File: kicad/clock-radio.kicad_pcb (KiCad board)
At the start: 4 copper layers, 214 x 122 mm, 49 parts, among them J1 Rotary Encoder Header, J2 Antenna, J3 USB_C_Receptacle_USB2.0_16P, J4 SWD Header, J5 Display Header, J6 Speaker Header, SW1 BOOT0, U1 DS3231MZ, U2 STM32G0B1CETx, U3 RDA5807M_Module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

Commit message: updated pcb layout
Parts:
- R13, R8, R9: footprint Resistor_SMD:R_0201_0603Metric_Pad0.64x0.40mm_HandSolder -> Resistor_SMD:R_0402_1005Metric_Pad0.72x0.64mm_HandSolder
- moved C20 73.1 mm to (161.1, 39.4), turned to 180 degrees
- moved R13 56.3 mm to (161.1, 38.0), turned to 180 degrees
- moved R1 51.8 mm to (148.4, 58.6), turned to 180 degrees
- moved R4 50.1 mm to (164.2, 57.0), turned to 90 degrees
- moved C17 49.4 mm to (161.2, 43.0)
- moved C4 49.4 mm to (167.0, 48.6), turned to 90 degrees
- moved C18 49.1 mm to (161.2, 41.4)
- moved R8 48.4 mm to (156.5, 46.6), turned to 90 degrees
- moved R6 48.3 mm to (162.6, 57.0), turned to 90 degrees
- moved R9 45.9 mm to (151.8, 46.6), turned to 90 degrees
- moved J2 45.8 mm to (133.2, 46.4)
- moved C3 39.8 mm to (156.8, 63.2)
- moved J1 39.3 mm to (125.6, 53.9)
- moved C1 38.3 mm to (155.4, 62.0), turned to 180 degrees
- moved C2 37.9 mm to (155.4, 60.8), turned to 180 degrees
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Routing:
- net GND: track 0.00 -> 30.5 mm, vias 0 -> 7
- net SDA: track 0.00 -> 25.0 mm, vias 0 -> 1
- net SCL: track 0.00 -> 25.0 mm, vias 0 -> 2
- net +3V3: track 0.00 -> 18.2 mm, vias 0 -> 2
- net RTC_INT: track 0.00 -> 16.9 mm, vias 0 -> 2
- net +5V: track 0.00 -> 15.3 mm, vias 0 -> 5
- net SWCLK: track 0.00 -> 6.53 mm
- net Net-(J3-SHIELD): track 0.00 -> 5.99 mm
- net Net-(U2-PF2): track 0.00 -> 4.82 mm
- net Net-(J3-CC1): track 0.00 -> 3.52 mm
- net Net-(J3-CC2): track 0.00 -> 3.13 mm
- net Net-(R1-Pad2): track 0.00 -> 2.40 mm
- net Net-(J3-D--PadA7): track 6.08 -> 4.77 mm
- added copper zone on F.Cu, net +5V
- added copper zone on F.Cu, net GND
- added copper zone on F.Cu, net Net-(U2-VBAT)
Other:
- board size 214 x 122 mm -> 35 x 35 mm

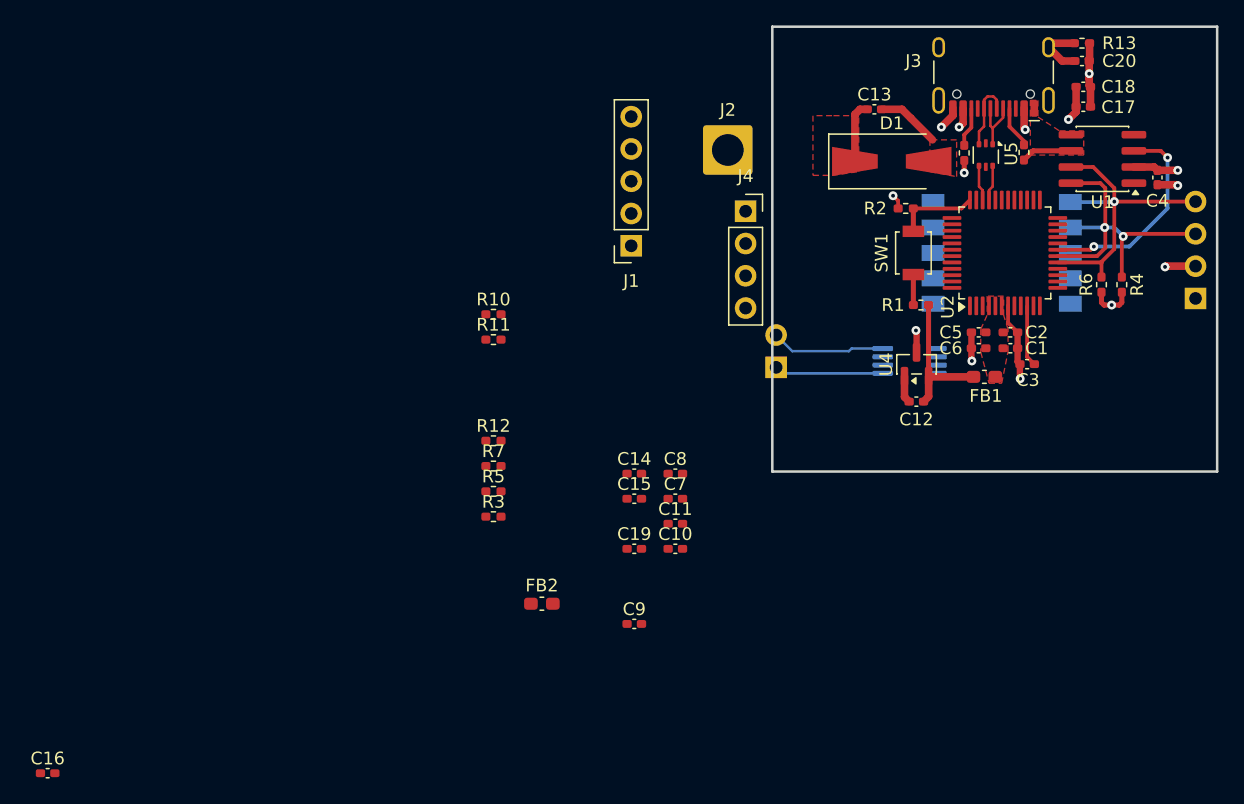
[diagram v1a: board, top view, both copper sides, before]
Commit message: connected all components and added in ground and power plane
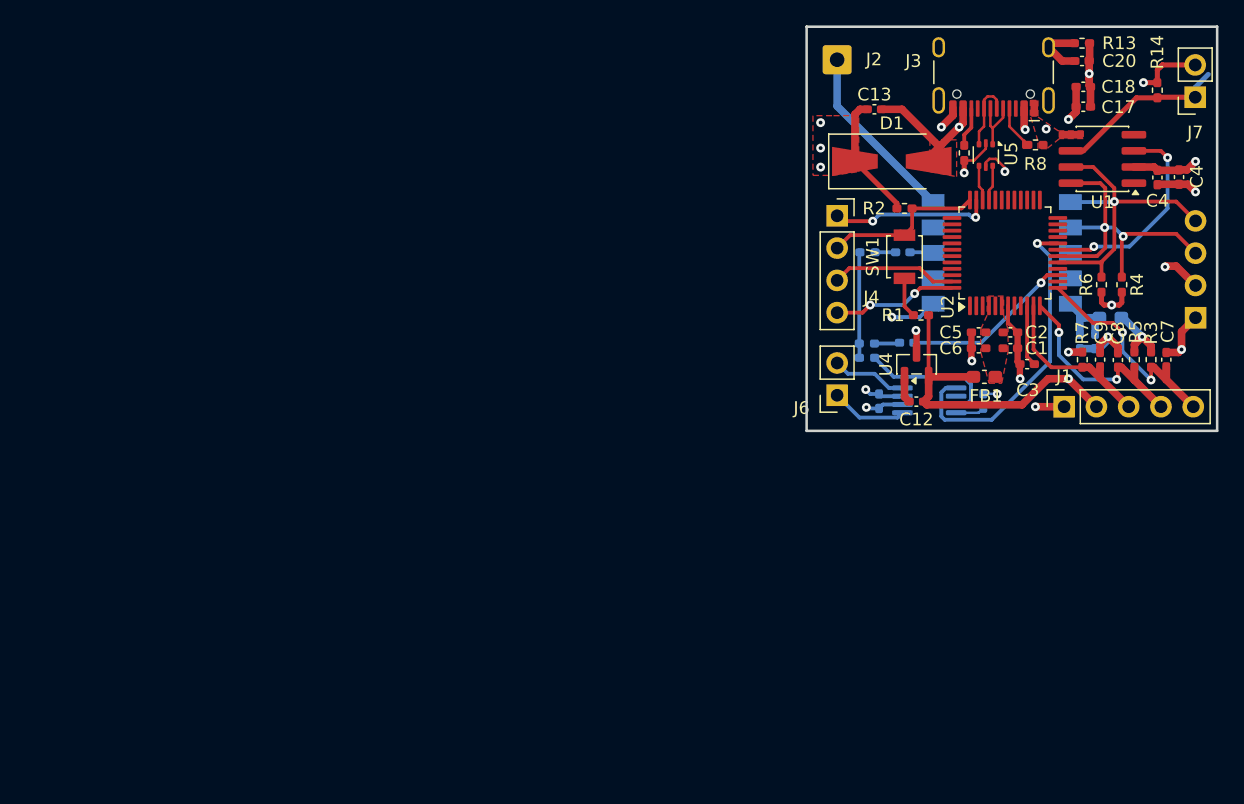
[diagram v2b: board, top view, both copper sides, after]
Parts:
- added C4: 100n, Capacitor_SMD:C_0402_1005Metric_Pad0.74x0.62mm_HandSolder, F.Cu at (168.7, 48.5)
- added J7: Coin Cell, Connector_PinSocket_2.54mm:PinSocket_1x02_P2.54mm_Vertical, F.Cu at (170.0, 42.2)
- added R14: 0, Resistor_SMD:R_0402_1005Metric_Pad0.72x0.64mm_HandSolder, F.Cu at (167.0, 41.7)
- C10, C11, C14, C15, C16, C19, FB2, R10, R11, R12: moved to B.Cu
- J2: footprint Connector_Wire:SolderWire-2sqmm_1x01_D2mm_OD3.9mm -> Connector_Wire:SolderWire-0.5sqmm_1x01_D0.9mm_OD2.3mm
- J6: moved to F.Cu
- moved C16 79.2 mm to (153.3, 66.2), turned to 90 degrees
- moved R3 53.2 mm to (166.5, 62.9), turned to 90 degrees
- moved R5 51.5 mm to (165.2, 62.9), turned to 90 degrees
- moved FB2 50.1 mm to (163.3, 59.6), turned to 180 degrees
- moved R7 47.1 mm to (161.1, 62.9), turned to 90 degrees
- moved C9 42.1 mm to (162.5, 62.9), turned to 90 degrees
- moved C7 40.1 mm to (167.7, 62.9), turned to 90 degrees
- moved C10 36.8 mm to (162.1, 61.5), turned to -90 degrees
- moved J1 36.3 mm to (159.7, 66.6), turned to 90 degrees
- moved C8 35.9 mm to (163.9, 62.9), turned to 90 degrees
- moved C11 34.9 mm to (160.9, 61.5), turned to -90 degrees
- moved R12 30.1 mm to (144.2, 62.8)
- moved R10 29.8 mm to (144.2, 54.5), turned to 180 degrees
- moved R11 29.4 mm to (144.1, 61.6)
- moved C14 27.4 mm to (147.0, 54.5), turned to 180 degrees
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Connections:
- U1 pad 6: GND -> Net-(J7-Pin_1)
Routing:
- net +5V: track 15.3 -> 62.5 mm, vias 5 -> 7
- net +3V3: track 18.2 -> 56.8 mm, vias 2 -> 5
- net GND: track 30.5 -> 61.5 mm, vias 7 -> 17
- net SD: track 0.00 -> 25.1 mm, vias 0 -> 1
- net Button: track 0.00 -> 17.8 mm, vias 0 -> 2
- net TIM2_CH2: track 0.00 -> 16.5 mm, vias 0 -> 2
- net Net-(J2-Pin_1): track 0.00 -> 14.3 mm
- net Net-(J7-Pin_1): track 0.00 -> 13.7 mm
- net TIM2_CH1: track 0.00 -> 13.7 mm
- net DAC1: track 0.00 -> 13.6 mm, vias 0 -> 1
- net SWDIO: track 0.00 -> 12.8 mm, vias 0 -> 2
- net Net-(U6-IN+): track 0.00 -> 11.0 mm
- net UART_TX: track 0.00 -> 9.87 mm
- net UART_RX: track 0.00 -> 9.85 mm, vias 0 -> 2
- net Net-(R10-Pad2): track 0.00 -> 8.26 mm
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- added copper zone on In2.Cu, net +3V3
- added copper zone on In2.Cu, net +5V
- added copper zone on In1.Cu, net GND
- added copper zone on In1.Cu, net Net-(J3-SHIELD)
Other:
- board size 35 x 35 mm -> 32.3 x 31.8 mm

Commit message: Check out antenna footprint
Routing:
- net GND: track 61.5 -> 65.3 mm
- net Net-(J7-Pin_1): track 13.7 -> 11.5 mm
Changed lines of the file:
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@@
 		(tags "Through hole socket strip THT 1x02 2.54mm single row")
 		(property "Reference" "J6"
-			(at 2.8 -1 0)
+			(at -3.2 -0.05 0)
 			(layer "F.SilkS")
 			(effects
@@
 		(tags "MSOP SO")
 		(property "Reference" "U6"
-			(at 0 2.45 0)
+			(at 0 2.2 0)
 			(layer "B.SilkS")
 			(effects
@@
 		(tags "resistor handsolder")
 		(property "Reference" "R12"
-			(at -2.7025 0 0)
+			(at -0.1525 1.25 0)
 			(layer "B.SilkS")
 			(effects
@@
 		(tags "resistor handsolder")
 		(property "Reference" "R11"
-			(at -2.690541 -0.028809 0)
+			(at -0.140541 -1.128809 0)
 			(layer "B.SilkS")
 			(effects
@@
 	)
 	(segment
+		(start 146.515 65.25)
+		(end 144.05 65.25)
+		(width 0.6)
+		(layer "F.Cu")
+		(net 1)
+	)
+	(segment
 		(start 169.4 49.1)
 		(end 170 49.7)
@@
 	)
 	(segment
+		(start 147.465 66.2)
+		(end 146.515 65.25)
+		(width 0.6)
+		(layer "F.Cu")
+		(net 1)
+	)
+	(segment
 		(start 153.5 45.875)
 		(end 153.5 46.3)
@@
 		(net 74)
 	)
-	(segment
-		(start 169.975 42.25)
-		(end 169.975 41.477767)
-		(width 0.4)
-		(layer "B.Cu")
-		(net 74)
-	)
-	(segment
-		(start 169.975 41.477767)
-		(end 171 40.452767)
-		(width 0.4)
-		(layer "B.Cu")
-		(net 74)
-	)

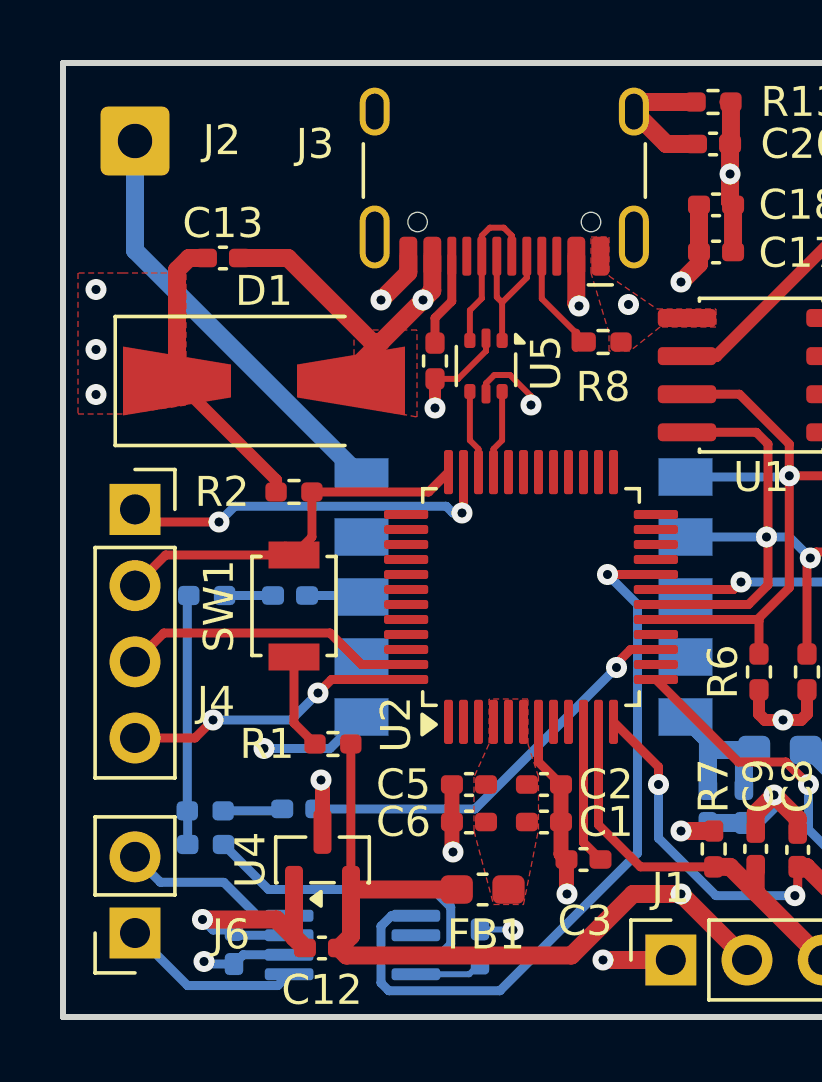
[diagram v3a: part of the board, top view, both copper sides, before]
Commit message: swapped layers
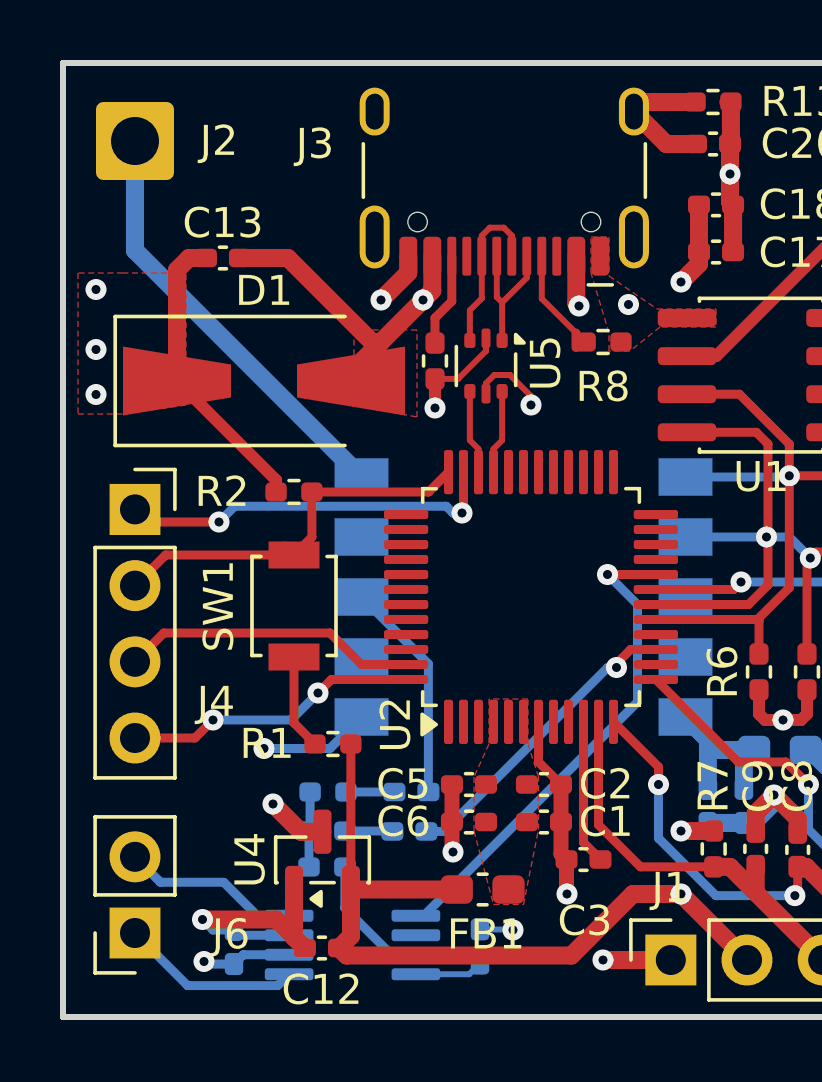
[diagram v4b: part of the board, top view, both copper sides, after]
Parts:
- J2: footprint Connector_Wire:SolderWire-0.5sqmm_1x01_D0.9mm_OD2.3mm -> Connector_Wire:SolderWire-0.75sqmm_1x01_D1.25mm_OD2.3mm
- moved R10 7.70 mm to (148.2, 61.0)
- moved C14 7.70 mm to (151.0, 61.0)
- moved R12 4.11 mm to (148.2, 63.5)
- moved R11 4.11 mm to (148.2, 62.3)
- moved C15 3.75 mm to (150.9, 62.3)
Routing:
- net +5V: track 62.5 -> 26.3 mm
- net +3V3: track 56.8 -> 41.0 mm
- net SD: track 25.1 -> 16.6 mm
- net Net-(U6-IN+): track 11.0 -> 4.38 mm
- net Net-(R10-Pad2): track 8.26 -> 2.52 mm
- net Net-(U3-LOUT): track 1.84 -> 7.49 mm
- net DAC1: track 13.6 -> 10.2 mm
- added copper zone on In1.Cu, net +3V3
- added copper zone on In1.Cu, net +5V
- added copper zone on In2.Cu, net GND
- added copper zone on In2.Cu, net Net-(J3-SHIELD)
- removed copper zone on In2.Cu, net +3V3
- removed copper zone on In2.Cu, net +5V
- removed copper zone on In1.Cu, net GND
- removed copper zone on In1.Cu, net Net-(J3-SHIELD)

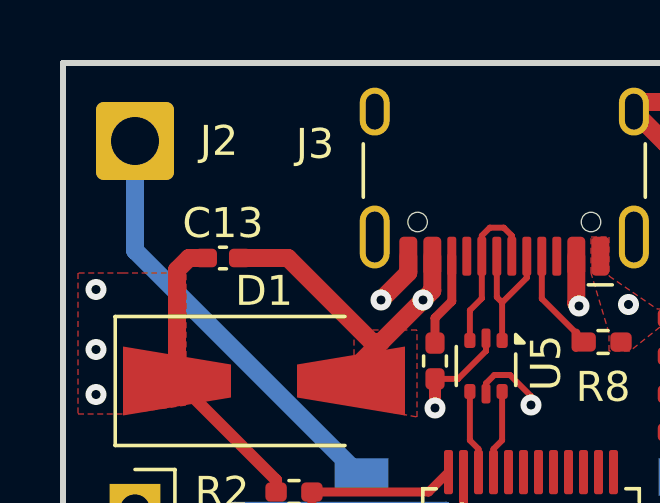
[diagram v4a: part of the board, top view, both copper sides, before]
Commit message: Added m2 hole
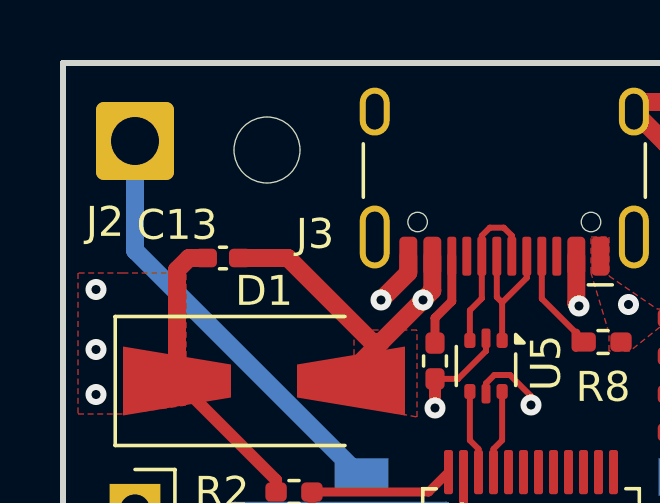
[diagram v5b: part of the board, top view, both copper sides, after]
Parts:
- added REF**: MountingHole_2.2mm_M2, MountingHole:MountingHole_2.2mm_M2, F.Cu at (146.2, 39.6)
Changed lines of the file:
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@@
 		(tags "connector wire 0.75sqmm")
 		(property "Reference" "J2"
-			(at 2.8 0 0)
+			(at -1 2.7 0)
 			(layer "F.SilkS")
 			(effects
@@
 		(tags "usb usb-c 2.0 pd")
 		(property "Reference" "J3"
-			(at 6.31 -0.005 180)
+			(at 6.31 -3.005 180)
 			(layer "F.SilkS")
 			(effects
@@
 		)
 	)
+	(footprint "MountingHole:MountingHole_2.2mm_M2"
+		(layer "F.Cu")
+		(at 146.2 39.6)
+		(descr "Mounting Hole 2.2mm, M2, no annular, generated by kicad-footprint-generator mountinghole.py")
+		(tags "mountinghole M2")
+		(property "Reference" "REF**"
+			(at 0 -3.15 0)
+			(layer "F.SilkS")
+			(hide yes)
+			(effects
+				(font
+					(size 1 1)
+					(thickness 0.15)
+				)
+			)
+		)
+		(property "Value" "MountingHole_2.2mm_M2"
+			(at 0 3.15 0)
+			(layer "F.Fab")
+			(effects
+				(font
+					(size 1 1)
+					(thickness 0.15)
+				)
+			)
+		)
+		(property "Datasheet" ""
+			(at 0 0 0)
+			(layer "F.Fab")
+			(hide yes)
+			(effects
+				(font
+					(size 1.27 1.27)
+					(thickness 0.15)
+				)
+			)
+		)
+		(property "Description" ""
+			(at 0 0 0)
+			(layer "F.Fab")
+			(hide yes)
+			(effects
+				(font
+					(size 1.27 1.27)
+					(thickness 0.15)
+				)
+			)
+		)
+		(attr exclude_from_pos_files exclude_from_bom)
+		(fp_circle
+			(center 0 0)
+			(end 2.2 0)
+			(stroke
+				(width 0.15)
+				(type solid)
+			)
+			(fill no)
+			(layer "Cmts.User")
+		)
+		(fp_circle
+			(center 0 0)
+			(end 2.45 0)
+			(stroke
+				(width 0.05)
+				(type solid)
+			)
+			(fill no)
+			(layer "F.CrtYd")
+		)
+		(fp_text user "${REFERENCE}"
+			(at 0 0 0)
+			(layer "F.Fab")
+			(effects
+				(font
+					(size 1 1)
+					(thickness 0.15)
+				)
+			)
+		)
+		(pad "" np_thru_hole circle
+			(at 0 0)
+			(size 2.2 2.2)
+			(drill 2.2)
+			(layers "*.Cu" "*.Mask")
+		)
+		(embedded_fonts no)
+	)
 	(footprint "Resistor_SMD:R_0402_1005Metric_Pad0.72x0.64mm_HandSolder"
 		(layer "F.Cu")
@@
 		(tags "capacitor handsolder")
 		(property "Reference" "C13"
-			(at 0 -1.16 0)
+			(at -1.5325 -1.1 0)
 			(layer "F.SilkS")
 			(effects
